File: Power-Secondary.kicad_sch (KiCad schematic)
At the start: 37 parts, among them J1 SUPP PWR MON, J2 SUPP PWR 1, J3 SUPP PWR 2, J4 DCDC SUPPLY, J5 FUSE OUT, J6 SUPP OUT, J7 LV ENABLE, Q1 S1G1D2S2G2D1, Q1A1 IRFU5305PbF, Q1A2 IRFU5305PbF, Q1A3 IRFU5305PbF, Q1A4 IRFU5305PbF, Q2 S1G1D2S2G2D1, Q3 FDD86250-F085

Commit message: early sch
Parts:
- removed C3: 100uF, Capacitor_SMD:C_1210_3225Metric, symbol Device:C
- removed D1: 10V, UTSVT_PowerSupp:SOD2512X110N, symbol Device:D_Zener
- removed DS1: SUPP_PWR, Diode_SMD:D_0805_2012Metric, symbol Device:LED
- removed DS2: DCDC_PWR, Diode_SMD:D_0805_2012Metric, symbol Device:LED
- removed F1: Fuse, Fuse:Fuseholder_Blade_Mini_Keystone_3568, symbol Device:Fuse
- removed H1, H2, H3, H4: M3, MountingHole:MountingHole_3mm, symbol Mechanical:MountingHole
- removed J1: SUPP PWR MON, Connector_Molex:Molex_Micro-Fit_3.0_43650-0215_1x02_P3.00mm_Vertical, symbol Connector:Conn_01x02_Pin
- removed J2: SUPP PWR 1, Connector_Molex:Molex_Sabre_43160-0102_1x02_P7.49mm_Vertical, symbol Connector:Conn_01x02_Pin
- removed J3: SUPP PWR 2, Connector_Molex:Molex_Sabre_43160-0102_1x02_P7.49mm_Vertical, symbol Connector:Conn_01x02_Pin
- removed J4: DCDC SUPPLY, Connector_Molex:Molex_Sabre_43160-0102_1x02_P7.49mm_Vertical, symbol Connector:Conn_01x02_Pin
- removed J5: FUSE OUT, Connector_Molex:Molex_Sabre_43160-0102_1x02_P7.49mm_Vertical, symbol Connector:Conn_01x02_Pin
- removed J6: SUPP OUT, Connector_Molex:Molex_Micro-Fit_3.0_43650-0215_1x02_P3.00mm_Vertical, symbol Connector:Conn_01x02_Pin
- removed J7: LV ENABLE, Connector_Molex:Molex_Micro-Fit_3.0_43650-0215_1x02_P3.00mm_Vertical, symbol Connector:Conn_01x02_Pin
- removed LOGO1: Dr Hallock, UTSVT_Special:Hallock_Image_Tiny, symbol utsvt-misc:Logo_Placeholder
- removed LOGO2: UTSVT, UTSVT_Special:UTSVT_Logo_Symbol, symbol utsvt-misc:Logo_Placeholder
- removed Q1: S1G1D2S2G2D1, UTSVT_PowerSupp:SOT65P210X100-6N, symbol Device:Q_Dual_PMOS_S1G1D2S2G2D1
- removed Q1A1, Q1A2, Q1A3, Q1A4: IRFU5305PbF, UTSVT_PowerSupp:SUP90P06-PCHAN-ENH-PWR-MOSFET, symbol utsvt-powersupp:SUP90P06-PCHANNEL-MOSFET
- removed Q2: S1G1D2S2G2D1, UTSVT_PowerSupp:SOT65P210X100-6N, symbol Device:Q_Dual_NMOS_S1G1D2S2G2D1
- removed Q3: FDD86250-F085, UTSVT_PowerSupp:FDD13AN06A0F085, symbol Simulation_SPICE:NMOS
- removed R1, R4: 5.1K, Resistor_SMD:R_0805_2012Metric, symbol Device:R_Small
- removed TP1: SUPP_PWR, TestPoint:TestPoint_Pad_2.0x2.0mm, symbol Connector:TestPoint
- removed TP2: DCDC_PWR, TestPoint:TestPoint_Pad_2.0x2.0mm, symbol Connector:TestPoint
- removed TP3: ZENER_GATE, TestPoint:TestPoint_Pad_2.0x2.0mm, symbol Connector:TestPoint
- removed TP4: DCDC_Gate, TestPoint:TestPoint_Pad_2.0x2.0mm, symbol Connector:TestPoint
- removed TP5: Supp_Gate, TestPoint:TestPoint_Pad_2.0x2.0mm, symbol Connector:TestPoint
- removed TP6: GND, TestPoint:TestPoint_Pad_2.0x2.0mm, symbol Connector:TestPoint
- added C3: C_Polarized, ECE319K:CP_Radial_Tantal200mil, symbol ECE319K:C_Polarized
- added C4, C5, C6, C7, C8: C, symbol Device:C
- added R1, R8: 42K, symbol Device:R
- added R10, R9: ~, symbol Device:R
- added R4, R5: 1M, symbol Device:R
- added R6: 52K, symbol Device:R
- added R7: 5.5K, symbol Device:R
- added U1: ~, symbol utsvt-powersupp:LTC4421
- C1, C2: value 100uF -> C; footprint Capacitor_SMD:C_1210_3225Metric -> (none)
- R2: value 10k -> 5.5K; footprint Resistor_SMD:R_0603_1608Metric -> (none)
- R3: value 1M -> 52K; footprint Resistor_SMD:R_0603_1608Metric -> (none)
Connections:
- net DCDC_Gate renamed OV1
- net OV1: now also R1.1, U1.10 (OV1)
- net FUSE_OUT: no longer names the net of C1.1
- net FUSE_OUT: now also U1.1 (CPO); no longer C2.1
- removed net GNDS: C1.2, C2.2, R3.2
- net SUPP_PWR renamed UVR1
- net UVR1: now also R3.2, U1.9 (UVR1)
- net ZENER_GATE renamed UVF1
- net UVF1: now also R4.2, U1.8 (UVF1)
- new net: C7.1, U1.11 (TMR1)
- new net: R10.1, U1.34 (OUT2)
- new net: R10.2, U1.33 (SENSE2)
- new net: C1.2, C3.1, C4.1, R9.1, U1.2 (CPOREF), U1.3 (OUT1), U1.36 (EXTV_CC)
- new net: C8.1, U1.26 (TMR2)
- new net: C6.1, U1.17 (INTV_CC)
- new net: C5.1, U1.19 (QUAL)
- new net GND: C3.2, C4.2, C5.2, C6.2, C7.2, C8.2, R1.2, R8.2, U1.35 (GND)
- new net OV2: R7.2, R8.1, U1.27 (OV2)
- new net UVF2: R5.2, R6.1, U1.29 (UVF2)
- new net UVR2: R6.2, R7.1, U1.28 (UVR2)
- new net V1: R4.1, U1.7 (V1)
- new net V2: R5.1
- new net nmos/Gate1: C2.1, U1.6 (GATE1)
- new net nmos/Source_Input1: C2.2, U1.5 (SOURCE1)
- new net nmos/Source_Output1: R9.2, U1.4 (SENSE1)
- no-connect marks 0 -> 2
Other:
- added sheet nmos (nmos.kicad_sch)
- note added: "- features a Power Path Controller IC (LTC4421)"
- note added: "I_LIM = 25mV / R_SENSE I_LIM = 1.25 * I_LOAD(MAX) Use Kelvin connections from the R_SENSE terminals to the LTC4421's SENSE and OUT pins"
- note added: "Main Battery (DC-DC Convertor)"
- note added: "Power Board Revision"
- note added: "R_Total = 1.1 x 10^6 R1 = (0.5 * R_Total) / V_OVRISE = 42K R2 = ((V_OVRISE / V_UVRISE) - 1) * R1 = 5.5K R3 = (V_UVRISE / V_UVFALL) (V_OVRISE / V_UVRISE) * R1 = 52K R4 = R1 * ((V_OVRISE / 0.5) - 1) - R3 - R2 = 1M Will change to 3 different resistor strings in the future Use petetiometer for software control?"
- note added: "Reference pg 16 on datasheet for value"
- note added: "Supplemental Batteries"
- note removed: "0"
- note removed: "1"
- note removed: "DCDC"
- note removed: "DCDC Gate"
- note removed: "Extra caps in case we need them for stabilization"
- note removed: "Fuse Out"
- note removed: "Logic Table"
- note removed: "Power Board"
- note removed: "Replaced op-amps with MOSFETs and inverters for logic as the slew rates of the op-amps were too slow. Added capacitors for the output."
- note removed: "Supp"
- note removed: "Supp Gate"
- note removed: "TEST POINTS / LEDS"
- note removed: "This board switches power to the fuse box between the DCDC power supply and the supplemental battery depending on whether the DCDC power is on or not."
- note removed: "Used op-amp circuitry to handle power handoff between DCDC and supplemental. Added an extra connector for the second supplemental battery."
- note removed: "Used zener diode to determine when switch occurs. With a 10V zener diode, at the min Vt, the switch occurs when DCDC is at 10.8 V. At max Vt, the switch occurs when DCDC is at 11.5V. Assuming DCDC is either 0 or 12, this will select DCDC when it is at 12 and supplemental when DCDC is at 0."
- note removed: "Version History"
- note removed: "v4.0"
- note removed: "v4.1"
- note removed: "v4.2"

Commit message: changes
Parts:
- removed C1, C2, C4, C5, C6, C7, C8: C, symbol Device:C
- removed C3: C_Polarized, ECE319K:CP_Radial_Tantal200mil, symbol ECE319K:C_Polarized
- removed R1, R8: 42K, symbol Device:R
- removed R10, R9: ~, symbol Device:R
- removed R2, R7: 5.5K, symbol Device:R
- removed R3, R6: 52K, symbol Device:R
- removed R4, R5: 1M, symbol Device:R
- removed U1: ~, symbol utsvt-powersupp:LTC4421
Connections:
- no-connect marks 2 -> 0
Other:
- added sheet LTC4421 (LTC4421.kicad_sch)
- note removed: "I_LIM = 25mV / R_SENSE I_LIM = 1.25 * I_LOAD(MAX) Use Kelvin connections from the R_SENSE terminals to the LTC4421's SENSE and OUT pins"
- note removed: "R_Total = 1.1 x 10^6 R1 = (0.5 * R_Total) / V_OVRISE = 42K R2 = ((V_OVRISE / V_UVRISE) - 1) * R1 = 5.5K R3 = (V_UVRISE / V_UVFALL) (V_OVRISE / V_UVRISE) * R1 = 52K R4 = R1 * ((V_OVRISE / 0.5) - 1) - R3 - R2 = 1M Will change to 3 different resistor strings in the future Use petetiometer for software control?"
- note removed: "Reference pg 16 on datasheet for value"

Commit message: Finished sch
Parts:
- added C1, C2: 10u, ECE319K:C_Axial_200mil, symbol ECE319K:C
- added D7, D8: D_TVS, symbol Device:D_TVS
- added J1, J2: PowerConn, UTSVT_Connectors:Molex_MicroFit3.0_1x2xP3.00mm_PolarizingPeg_Vertical, symbol Connector_Generic:Conn_01x02
- added Q1, Q2, Q3, Q4: ~, symbol Power-Board:SQJQ142E-T1_GE3
- added R17, R18: 1.2, symbol Device:R
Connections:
- new net: C1.1, R17.2
- new net: C2.1, R18.2
- new net GND: C1.2, C2.2, D7.2 (A2), D8.2 (A2), J1.2 (Pin_2), J2.2 (Pin_2)
- new net LTC4421/GATE1: Q1.2 (Gate), Q2.2 (Gate)
- new net LTC4421/GATE2: Q3.2 (Gate), Q4.2 (Gate)
- new net LTC4421/OUT: Q2.3 (Source), Q4.3 (Source)
- new net LTC4421/V1: D7.1 (A1), J1.1 (Pin_1), Q1.3 (Source), R17.1
- new net LTC4421/V2: D8.1 (A1), J2.1 (Pin_1), Q3.3 (Source), R18.1
- new net SOURCE1: Q1.1 (Drain), Q2.1 (Drain)
- new net SOURCE2: Q3.1 (Drain), Q4.1 (Drain)
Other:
- removed sheet nmos
- sheet LTC4421 ports: added GATE1, GATE2, OUT, SOURCE1, SOURCE2, V1, V2; removed none

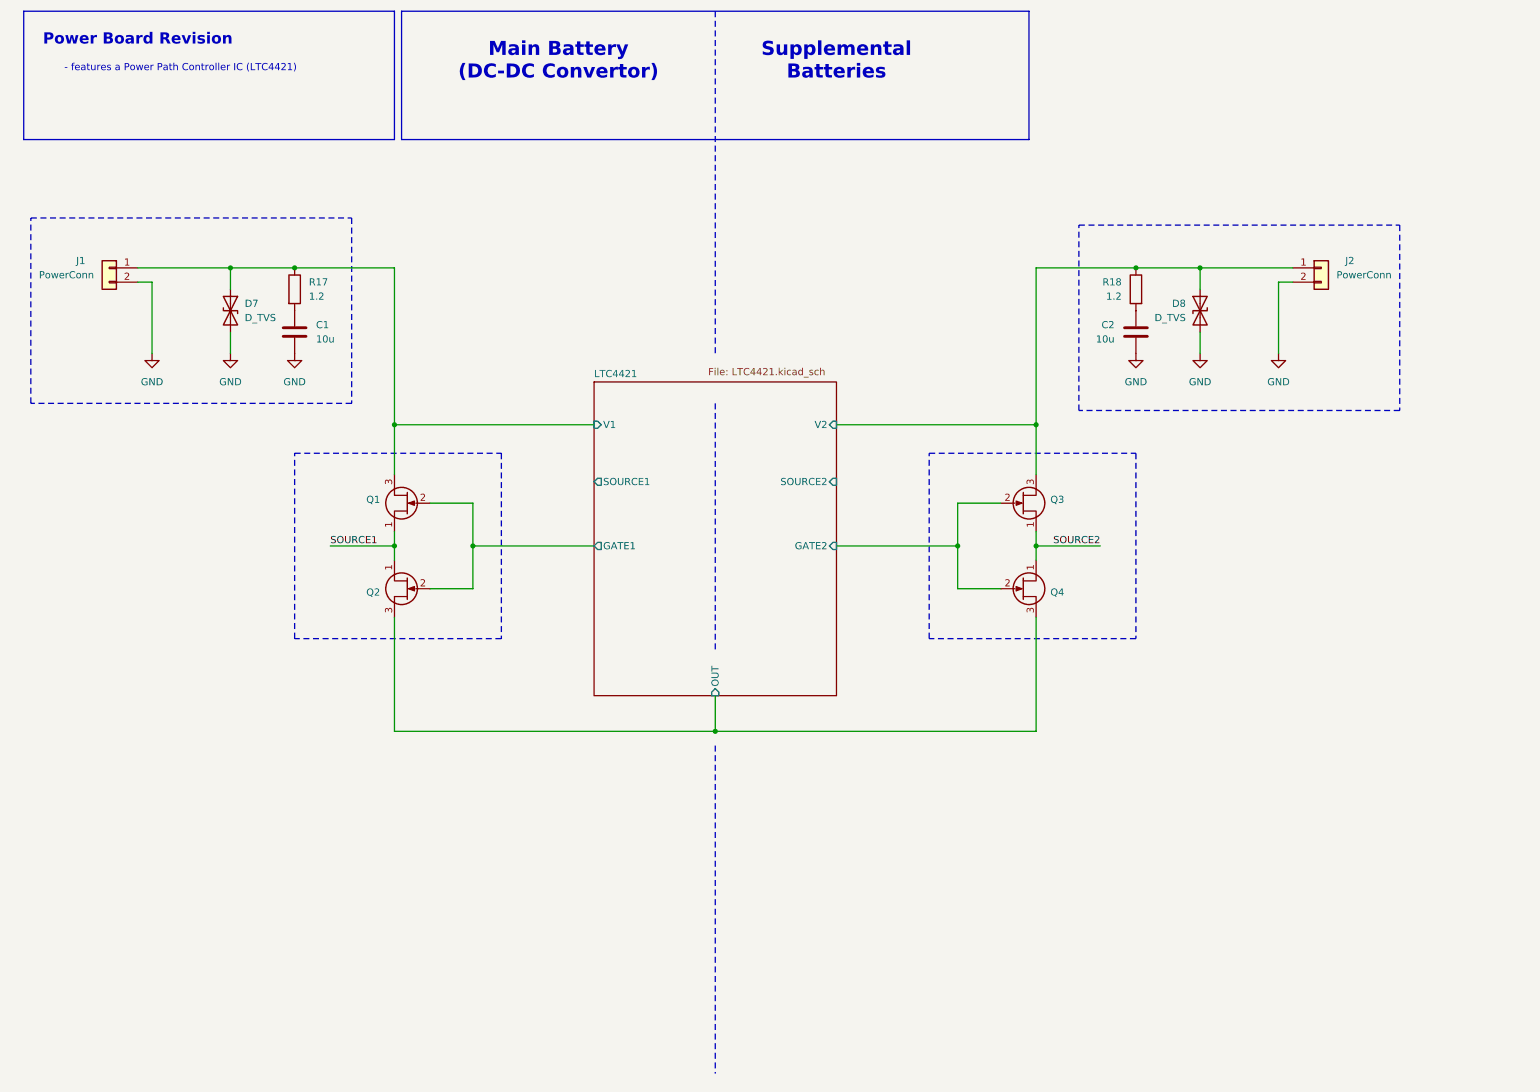
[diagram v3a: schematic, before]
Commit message: footprint assignments
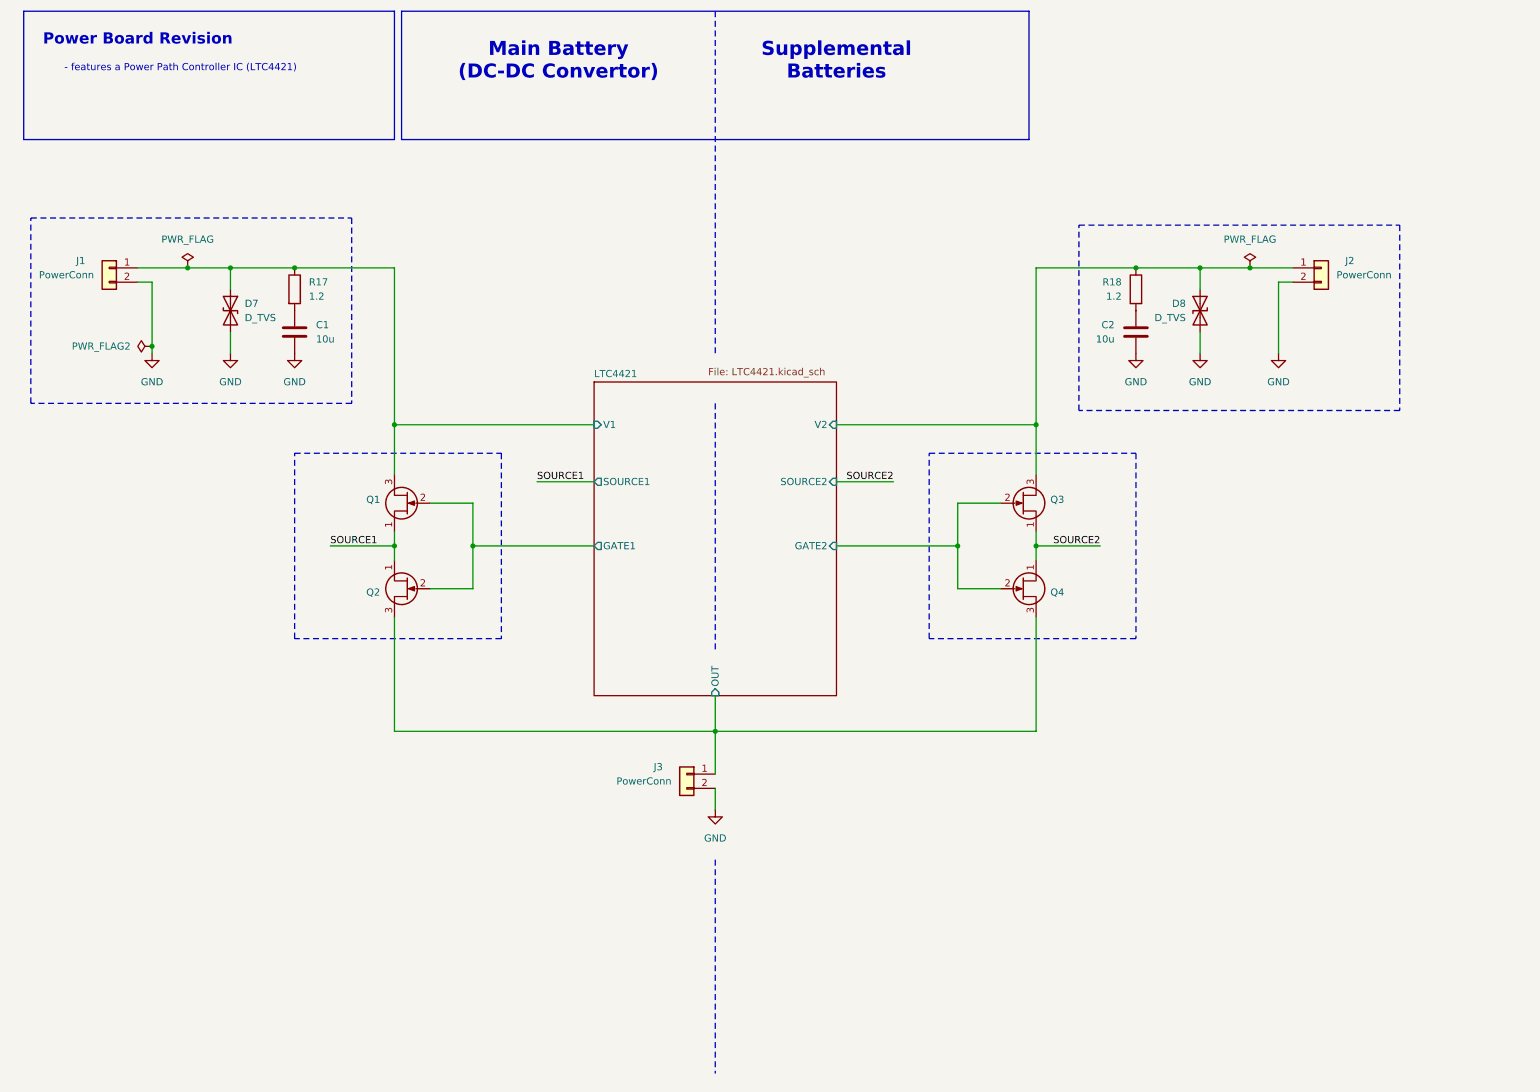
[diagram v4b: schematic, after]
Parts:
- added J3: PowerConn, symbol Connector_Generic:Conn_01x02
- C1, C2: footprint ECE319K:C_Axial_200mil -> Capacitor_SMD:C_0805_2012Metric
- D7, D8: footprint (none) -> Diode_SMD:D_SMA
- J1, J2: footprint UTSVT_Connectors:Molex_MicroFit3.0_1x2xP3.00mm_PolarizingPeg_Vertical -> (none)
- R17, R18: footprint (none) -> Resistor_SMD:R_0805_2012Metric
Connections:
- net GND: now also J3.2 (Pin_2)
- net LTC4421/OUT: now also J3.1 (Pin_1)

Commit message: changes to Power Board sch
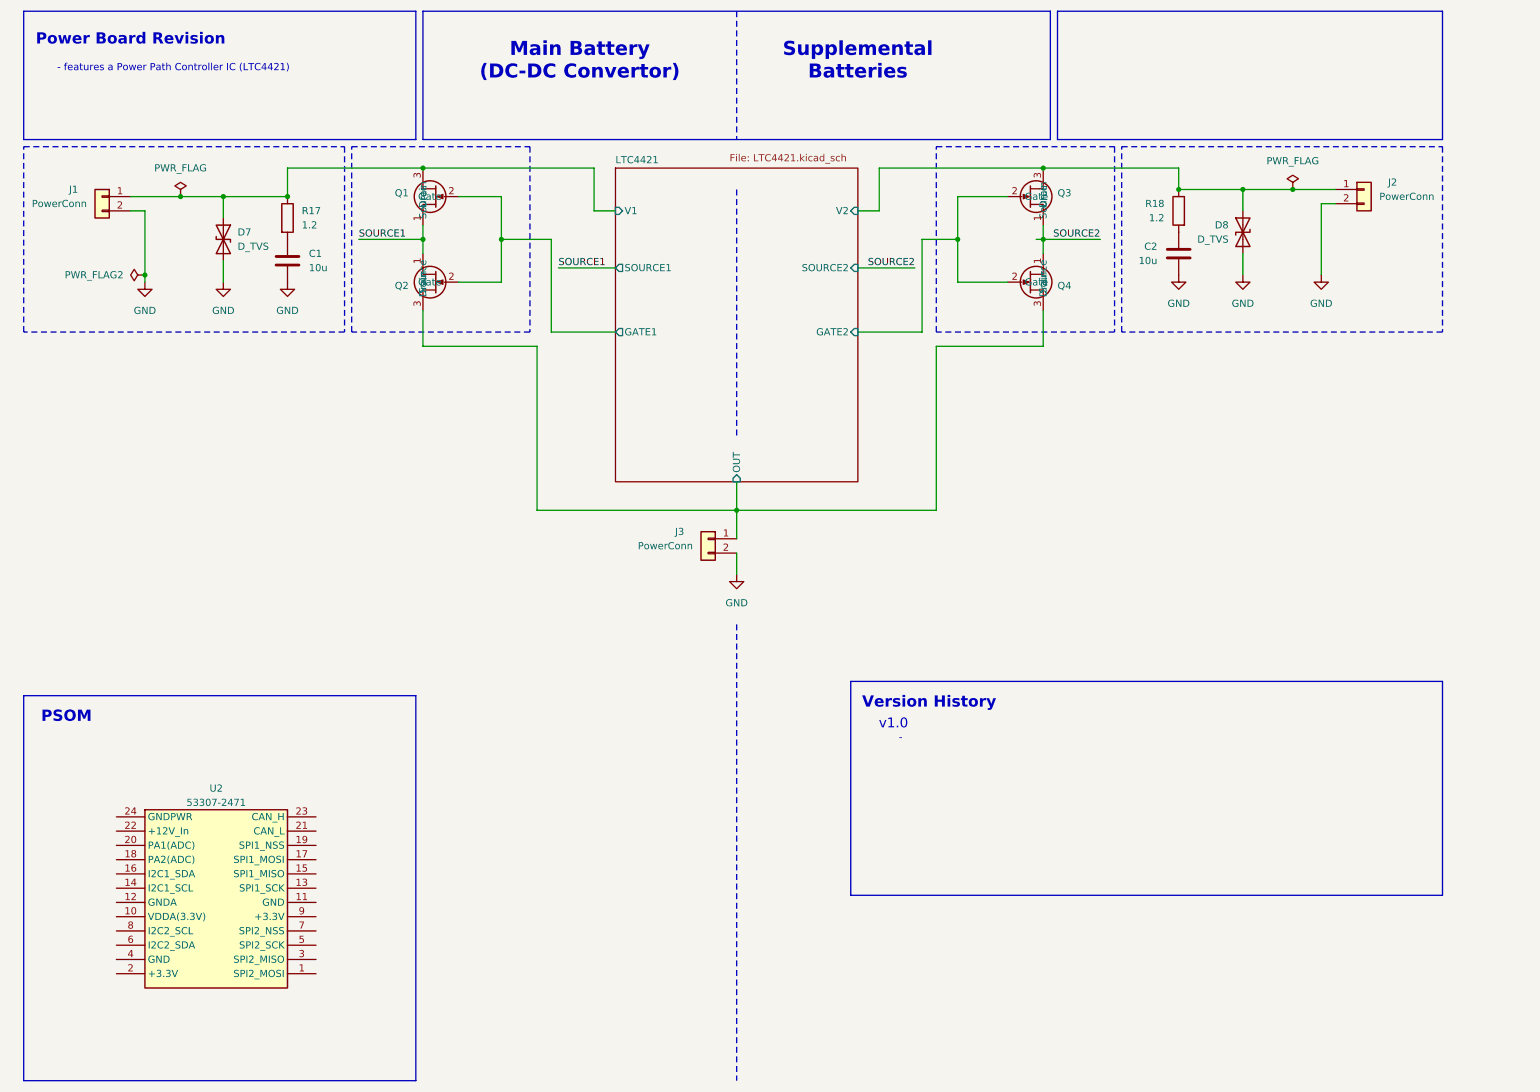
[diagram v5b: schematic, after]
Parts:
- added U2: ~, UTSVT_Special:PeripheralSOM, symbol utsvt-misc:PeripheralSOM
- C1, C2: footprint Capacitor_SMD:C_0805_2012Metric -> ECE319K:C_Axial_200mil
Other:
- note added: "-"
- note added: "PSOM"
- note added: "Version History"
- note added: "v1.0"
- moved on the sheet: C1, C2, D7, D8, J1, J2, J3, R17, R18

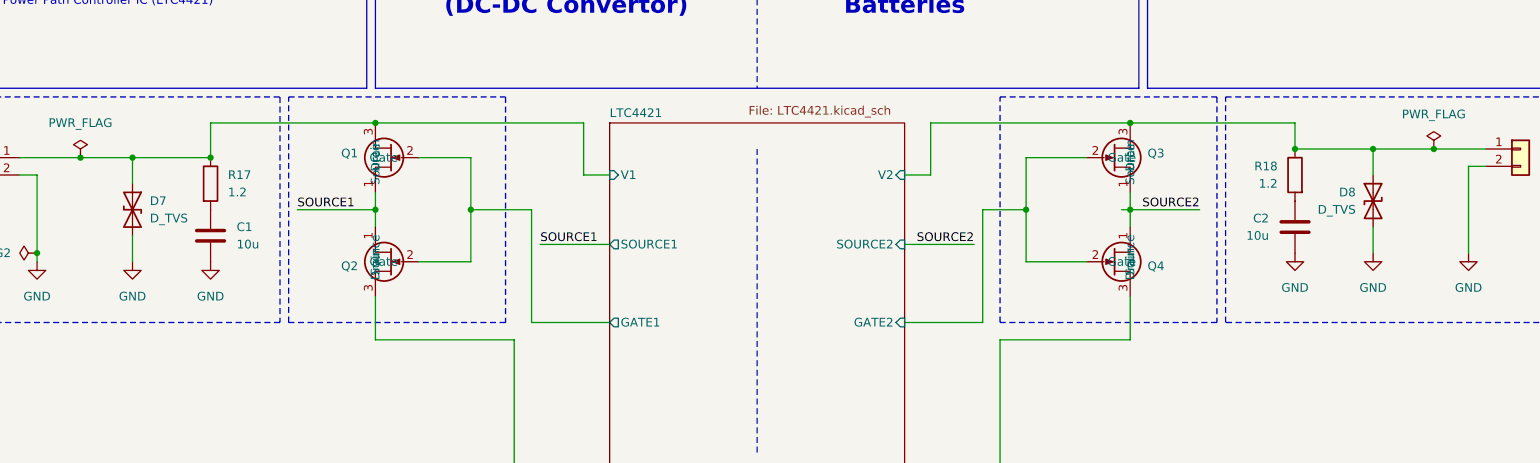
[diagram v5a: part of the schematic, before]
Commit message: CAD models, symbols update, and footprints
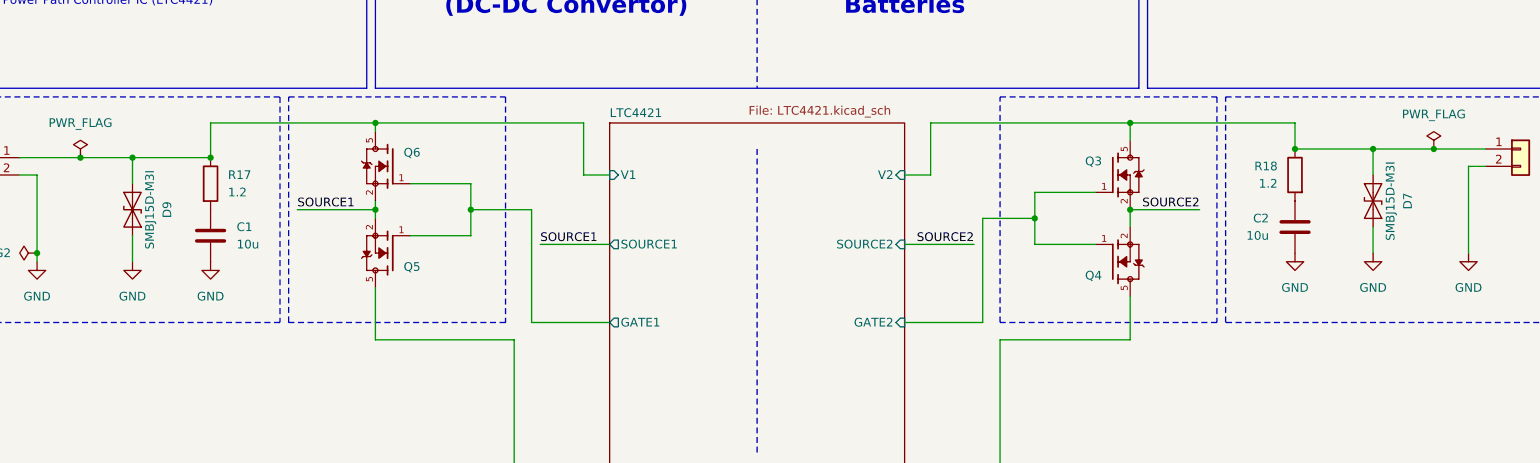
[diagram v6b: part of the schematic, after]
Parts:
- removed D7, D8: D_TVS, Diode_SMD:D_SMA, symbol Device:D_TVS
- removed Q1, Q2, Q3, Q4: ~, symbol Power-Board:SQJQ142E-T1_GE3
- added D7, D9: SMBJ15D-M3I, SMBJ15D-M3I:P26_DO-214AA_SMB, symbol SMBJ15D-M3I:SMBJ15D-M3I
- added Q3, Q4, Q5, Q6: SQJQ140E-T1_GE3, SQJQ140E-T1_GE3:TO200P800X182-5N, symbol SQJQ140E-T1_GE3:SQJQ140E-T1_GE3
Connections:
- net GND: now also D7.2 (A), D9.2 (A)
- net LTC4421/GATE1: now also Q5.1, Q6.1
- net LTC4421/GATE2: now also Q3.1, Q4.1
- net LTC4421/OUT: now also Q4.5, Q5.5
- net LTC4421/V1: now also D9.1 (K), Q6.5
- net LTC4421/V2: now also D7.1 (K), Q3.5
- net SOURCE1: now also Q5.2, Q5.3, Q5.4, Q6.2, Q6.3, Q6.4
- net SOURCE2: now also Q3.2, Q3.3, Q3.4, Q4.2, Q4.3, Q4.4
